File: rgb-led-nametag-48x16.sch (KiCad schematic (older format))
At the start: 44 parts, among them J1 USB_C_Receptacle_USB2.0, Q17 CJ3139K, Q18 CJ3139K, Q19 2SK3541, Q20 AO3401A, U25 STM32F722RETx, U26 SRV05-4, U27 TPS63001, U28 XC6206P332MR

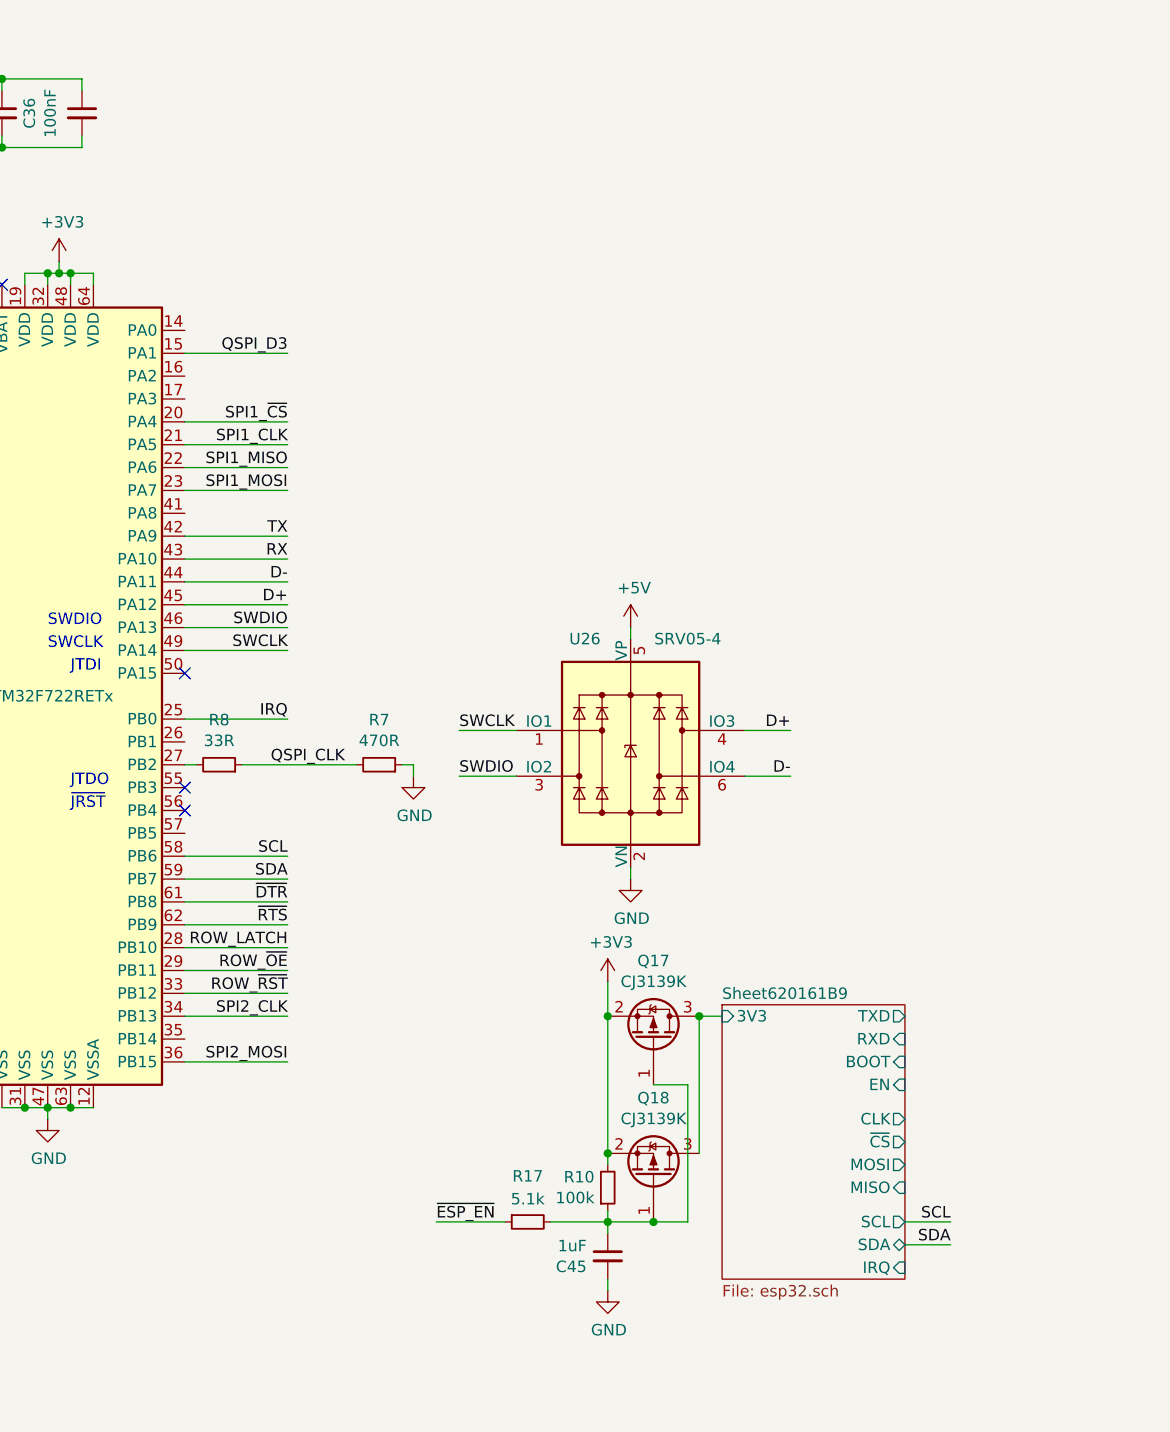
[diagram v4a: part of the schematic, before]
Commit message: Layout remaining busses
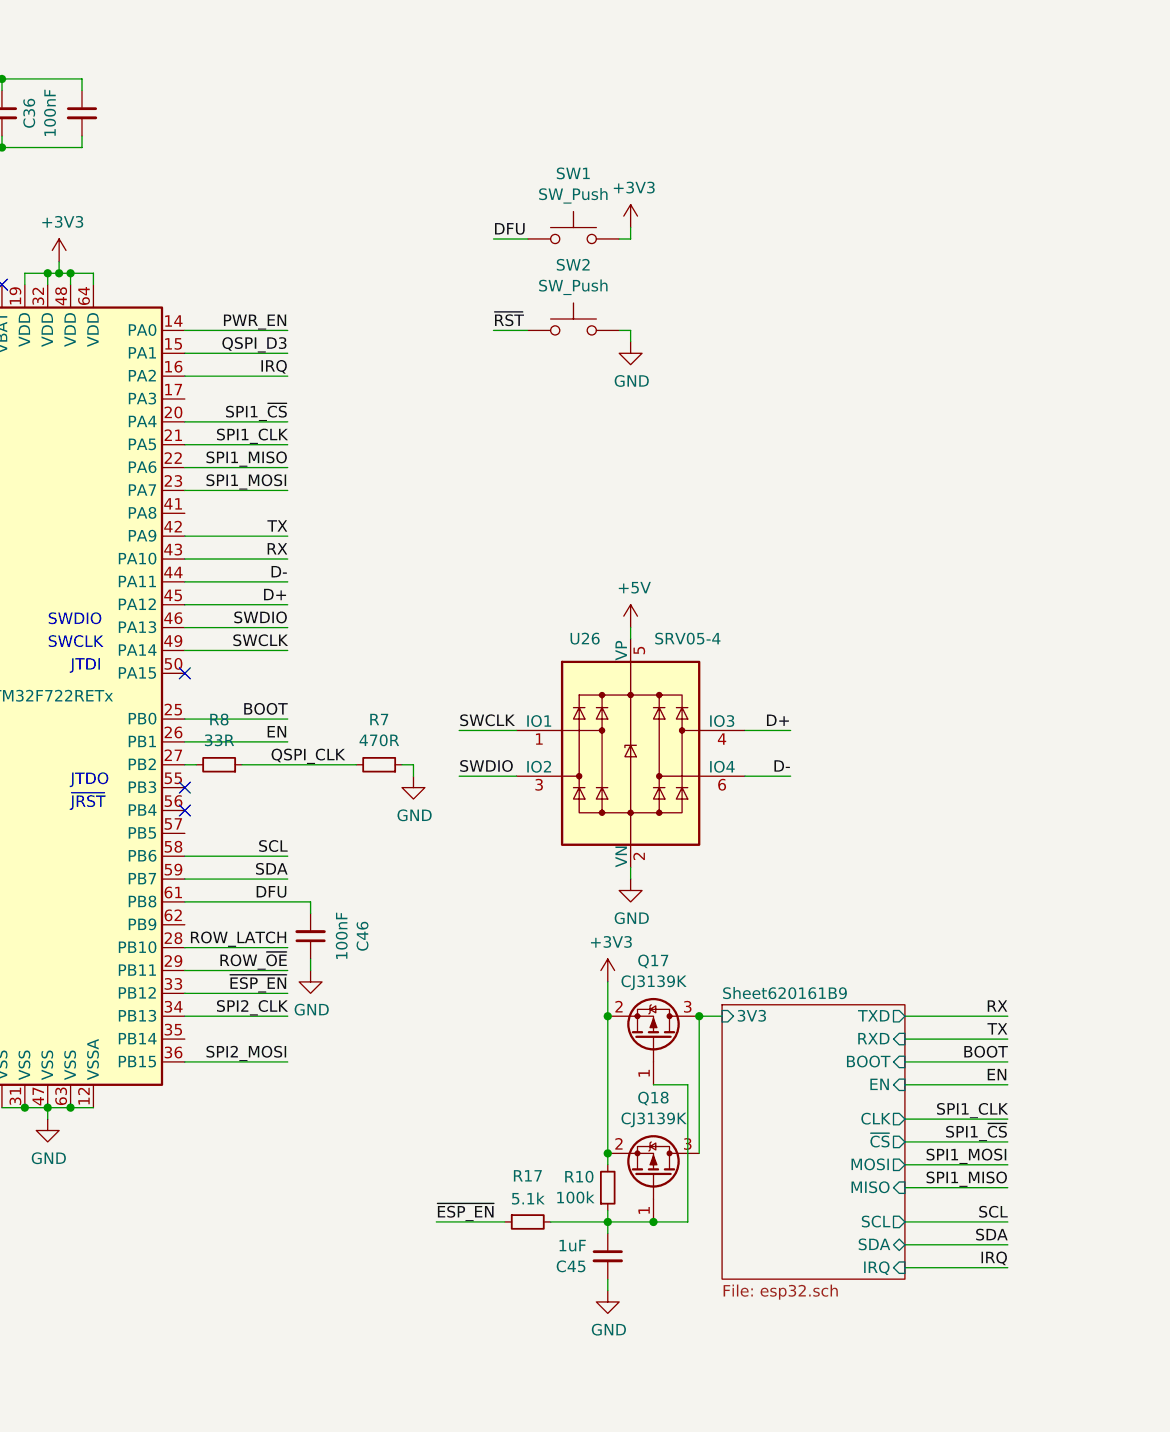
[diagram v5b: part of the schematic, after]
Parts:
- added C46: 100nF, Capacitor_SMD:C_0402_1005Metric, symbol Device:C_Small
- added SW1, SW2: SW_Push, Button_Switch_SMD:SW_Push_SPST_NO_Alps_SKRK, symbol Switch:SW_Push
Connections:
- net ROW_~RST is gone; now on net ~ESP_EN: U25.33 (PB12)
- net ~DTR is gone; now on net DFU: U25.61 (PB8)
- net +3V3: now also SW1.2
- net DFU: now also C46.2, SW1.1
- net GND: now also C46.1, SW2.2
- net IRQ: now also U25.16 (PA2); no longer U25.25 (PB0)
- net PWR_EN: now also U25.14 (PA0)
- net ~RST: now also SW2.1
- net EN: now reaches U25.26 (PB1)
- net ~RTS: no longer names the net of U25.62 (PB9)
- new net BOOT: U25.25 (PB0)
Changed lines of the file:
@@
 Text Label 7850 4450 2    50   ~ 0
 SDA
-Text Label 7850 4550 2    50   ~ 0
-~DTR
-Text Label 7850 4650 2    50   ~ 0
-~RTS
 Text Label 7850 3150 2    50   ~ 0
 D-
@@
 	7400 4450 7850 4450
 Wire Wire Line
-	7400 4550 7850 4550
-Wire Wire Line
-	7400 4650 7850 4650
-Wire Wire Line
 	7400 2750 7850 2750
 Wire Wire Line
@@
 Text Label 5650 4550 0    50   ~ 0
 COL_~RST
-Text Label 7850 4950 2    50   ~ 0
-ROW_~RST
-Wire Wire Line
-	7400 4950 7850 4950
 NoConn ~ 7400 3550
 Text Notes 6900 3550 0    50   ~ 0
@@
 NoConn ~ 7400 4150
 Wire Wire Line
-	7400 3750 7850 3750
-Text Label 7850 3750 2    50   ~ 0
+	7400 2250 7850 2250
+Text Label 7850 2250 2    50   ~ 0
 IRQ
 Wire Wire Line
@@
 	13250 950  13250 1000
 Connection ~ 13250 1000
-Text Label 10750 5950 2    50   ~ 0
+Text Label 11000 5950 2    50   ~ 0
 SCL
-Text Label 10750 6050 2    50   ~ 0
+Text Label 11000 6050 2    50   ~ 0
 SDA
-Wire Wire Line
-	10750 5950 10550 5950
-Wire Wire Line
-	10750 6050 10550 6050
 Wire Wire Line
 	14700 3600 15650 3600
@@
 Wire Wire Line
 	7400 5050 7850 5050
+Wire Wire Line
+	7400 4750 7850 4750
+Wire Wire Line
+	9350 4450 9350 4400
+Text Label 7850 5250 2    50   ~ 0
+SPI2_MOSI
+Wire Wire Line
+	7400 5250 7850 5250
+Wire Wire Line
+	7400 3850 7850 3850
+Text Label 11000 5350 2    50   ~ 0
+EN
+Text Label 7850 3850 2    50   ~ 0
+EN
 Text Label 7850 5050 2    50   ~ 0
 SPI2_CLK
-Wire Wire Line
-	7400 4750 7850 4750
 Text Label 7850 4750 2    50   ~ 0
 ROW_LATCH
 Wire Wire Line
-	9350 4450 9350 4400
+	7400 3750 7850 3750
+Text Label 7850 3750 2    50   ~ 0
+BOOT
+Text Label 11000 5250 2    50   ~ 0
+BOOT
+Text Label 11000 6150 2    50   ~ 0
+IRQ
+Text Label 11000 5500 2    50   ~ 0
+SPI1_CLK
+Text Label 11000 5600 2    50   ~ 0
+SPI1_~CS
+Text Label 11000 5800 2    50   ~ 0
+SPI1_MISO
+Text Label 11000 5700 2    50   ~ 0
+SPI1_MOSI
+Wire Wire Line
+	10550 5700 11000 5700
+Wire Wire Line
+	10550 5800 11000 5800
+Wire Wire Line
+	10550 5500 11000 5500
+Wire Wire Line
+	10550 5600 11000 5600
+Wire Wire Line
+	10550 5950 11000 5950
+Wire Wire Line
+	10550 6050 11000 6050
+Wire Wire Line
+	10550 6150 11000 6150
+Wire Wire Line
+	10550 5350 11000 5350
+Wire Wire Line
+	10550 5250 11000 5250
+Wire Wire Line
+	10550 5150 11000 5150
+Text Label 11000 5150 2    50   ~ 0
+TX
+Wire Wire Line
+	10550 5050 11000 5050
+Text Label 11000 5050 2    50   ~ 0
+RX
+Wire Wire Line
+	7400 4950 7850 4950
+Text Label 7850 4950 2    50   ~ 0
+~ESP_EN
+Wire Wire Line
+	7400 2050 7850 2050
+Text Label 7850 2050 2    50   ~ 0
+PWR_EN
+$Comp
+L Switch:SW_Push SW2
+U 1 1 630C4584
+P 9100 2050
+F 0 "SW2" H 9100 2335 50  0000 C CNN
+F 1 "SW_Push" H 9100 2244 50  0000 C CNN
+F 2 "Button_Switch_SMD:SW_Push_SPST_NO_Alps_SKRK" H 9100 2250 50  0001 C CNN
+F 3 "~" H 9100 2250 50  0001 C CNN
+F 4 "C115357" H 9100 2050 50  0001 C CNN "LCSC"
+	1    9100 2050
+	1    0    0    -1
+$EndComp
+$Comp
+L Switch:SW_Push SW1
+U 1 1 630C4D6E
+P 9100 1650
+F 0 "SW1" H 9100 1935 50  0000 C CNN
+F 1 "SW_Push" H 9100 1844 50  0000 C CNN
+F 2 "Button_Switch_SMD:SW_Push_SPST_NO_Alps_SKRK" H 9100 1850 50  0001 C CNN
+F 3 "~" H 9100 1850 50  0001 C CNN
+F 4 "C115357" H 9100 1650 50  0001 C CNN "LCSC"
+	1    9100 1650
+	1    0    0    -1
+$EndComp
+$Comp
+L power:GND #PWR0203
+U 1 1 630DD49F
+P 9350 2100
+F 0 "#PWR0203" H 9350 1850 50  0001 C CNN
+F 1 "GND" H 9355 1927 50  0000 C CNN
+F 2 "" H 9350 2100 50  0001 C CNN
+F 3 "" H 9350 2100 50  0001 C CNN
+	1    9350 2100
+	1    0    0    -1
+$EndComp
+Wire Wire Line
+	9350 2050 9300 2050
+Text Label 8750 2050 0    50   ~ 0
+~RST
+Wire Wire Line
+	8750 2050 8900 2050
+Text Label 8750 1650 0    50   ~ 0
+DFU
+Wire Wire Line
+	8750 1650 8900 1650
+Wire Wire Line
+	9350 2100 9350 2050
+$Comp
+L power:+3V3 #PWR0204
+U 1 1 631717FF
+P 9350 1600
+F 0 "#PWR0204" H 9350 1450 50  0001 C CNN
+F 1 "+3V3" H 9365 1773 50  0000 C CNN
+F 2 "" H 9350 1600 50  0001 C CNN
+F 3 "" H 9350 1600 50  0001 C CNN
+	1    9350 1600
+	1    0    0    -1
+$EndComp
+Wire Wire Line
+	9350 1600 9350 1650
+Wire Wire Line
+	9350 1650 9300 1650
+Text Label 7850 4550 2    50   ~ 0
+DFU
+$Comp
+L Device:C_Small C?
+U 1 1 631C20EA
+P 7950 4700
+AR Path="/61A41C1D/61A5C767/631C20EA" Ref="C?"  Part="1"
+AR Path="/61A41C1D/61A68DB0/631C20EA" Ref="C?"  Part="1"
+AR Path="/61A41C1D/61A6C361/631C20EA" Ref="C?"  Part="1"
+AR Path="/61A41C1D/61A75B5D/631C20EA" Ref="C?"  Part="1"
+AR Path="/61A41C1D/61A75B6D/631C20EA" Ref="C?"  Part="1"
+AR Path="/61A41C1D/61A75B93/631C20EA" Ref="C?"  Part="1"
+AR Path="/61C4C20D/61A5C767/631C20EA" Ref="C?"  Part="1"
+AR Path="/61C4C20D/61A68DB0/631C20EA" Ref="C?"  Part="1"
+AR Path="/61C4C20D/61A6C361/631C20EA" Ref="C?"  Part="1"
+AR Path="/61C4C20D/61A75B5D/631C20EA" Ref="C?"  Part="1"
+AR Path="/61C4C20D/61A75B6D/631C20EA" Ref="C?"  Part="1"
+AR Path="/61C4C20D/61A75B93/631C20EA" Ref="C?"  Part="1"
+AR Path="/61C4C905/61A5C767/631C20EA" Ref="C?"  Part="1"
+AR Path="/61C4C905/61A68DB0/631C20EA" Ref="C?"  Part="1"
+AR Path="/61C4C905/61A6C361/631C20EA" Ref="C?"  Part="1"
+AR Path="/61C4C905/61A75B5D/631C20EA" Ref="C?"  Part="1"
+AR Path="/61C4C905/61A75B6D/631C20EA" Ref="C?"  Part="1"
+AR Path="/61C4C905/61A75B93/631C20EA" Ref="C?"  Part="1"
+AR Path="/631C20EA" Ref="C46"  Part="1"
+F 0 "C46" V 7721 4700 50  0000 C CNN
+F 1 "100nF" V 7812 4700 50  0000 C CNN
+F 2 "Capacitor_SMD:C_0402_1005Metric" H 7950 4700 50  0001 C CNN
+F 3 "~" H 7950 4700 50  0001 C CNN
+F 4 "C1525" V 7950 4700 50  0001 C CNN "LCSC"
+	1    7950 4700
+	-1   0    0    1
+$EndComp
+Wire Wire Line
+	7950 4550 7950 4600
+Wire Wire Line
+	7400 4550 7950 4550
+$Comp
+L power:GND #PWR0205
+U 1 1 631F3184
+P 7950 4850
+F 0 "#PWR0205" H 7950 4600 50  0001 C CNN
+F 1 "GND" H 7955 4677 50  0000 C CNN
+F 2 "" H 7950 4850 50  0001 C CNN
+F 3 "" H 7950 4850 50  0001 C CNN
+	1    7950 4850
+	1    0    0    -1
+$EndComp
+Wire Wire Line
+	7950 4850 7950 4800
 Wire Bus Line
 	2950 1250 2950 6650
-Text Label 7850 5250 2    50   ~ 0
-SPI2_MOSI
-Wire Wire Line
-	7400 5250 7850 5250
 $EndSCHEMATC

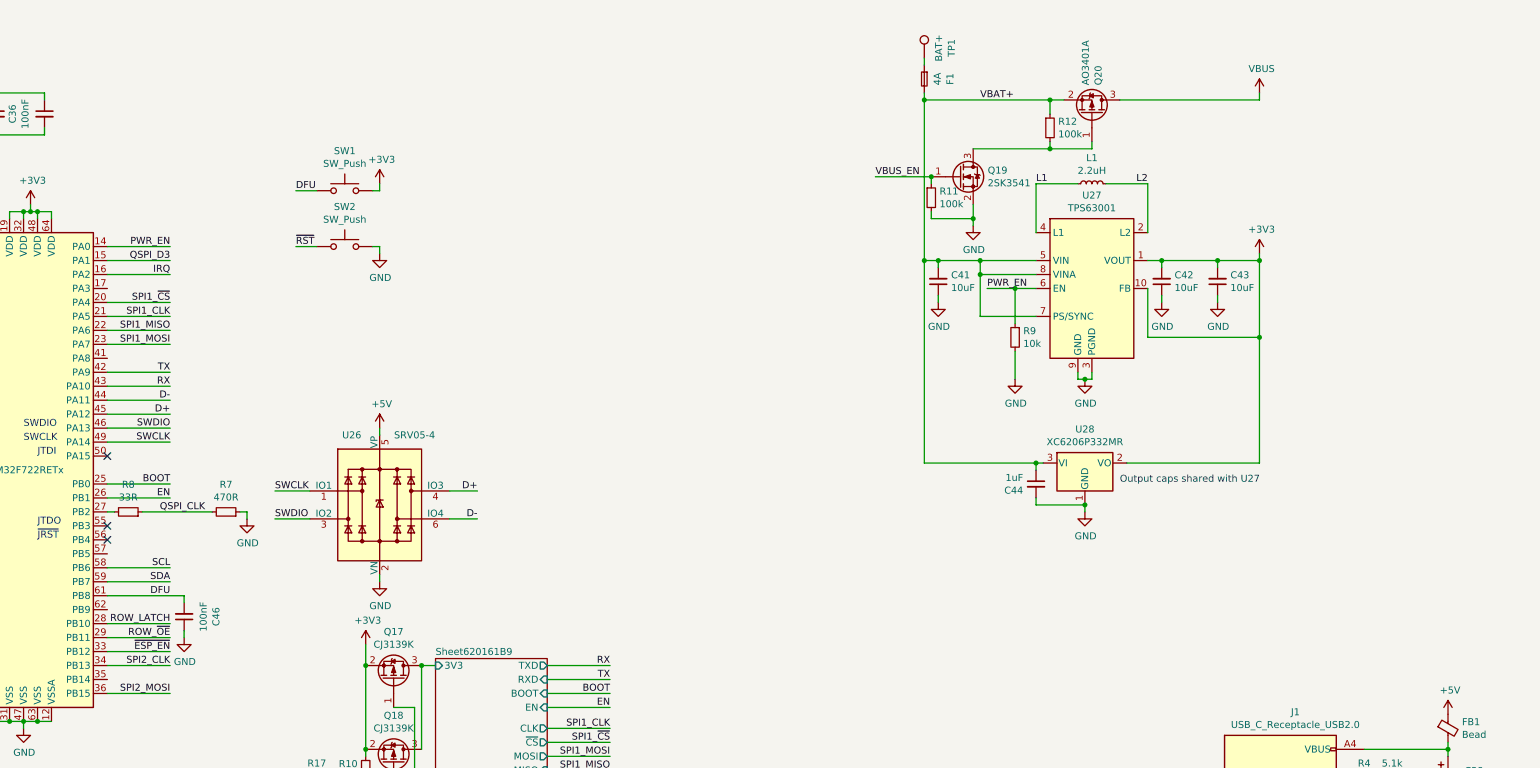
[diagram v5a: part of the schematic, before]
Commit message: Add primary battery protection
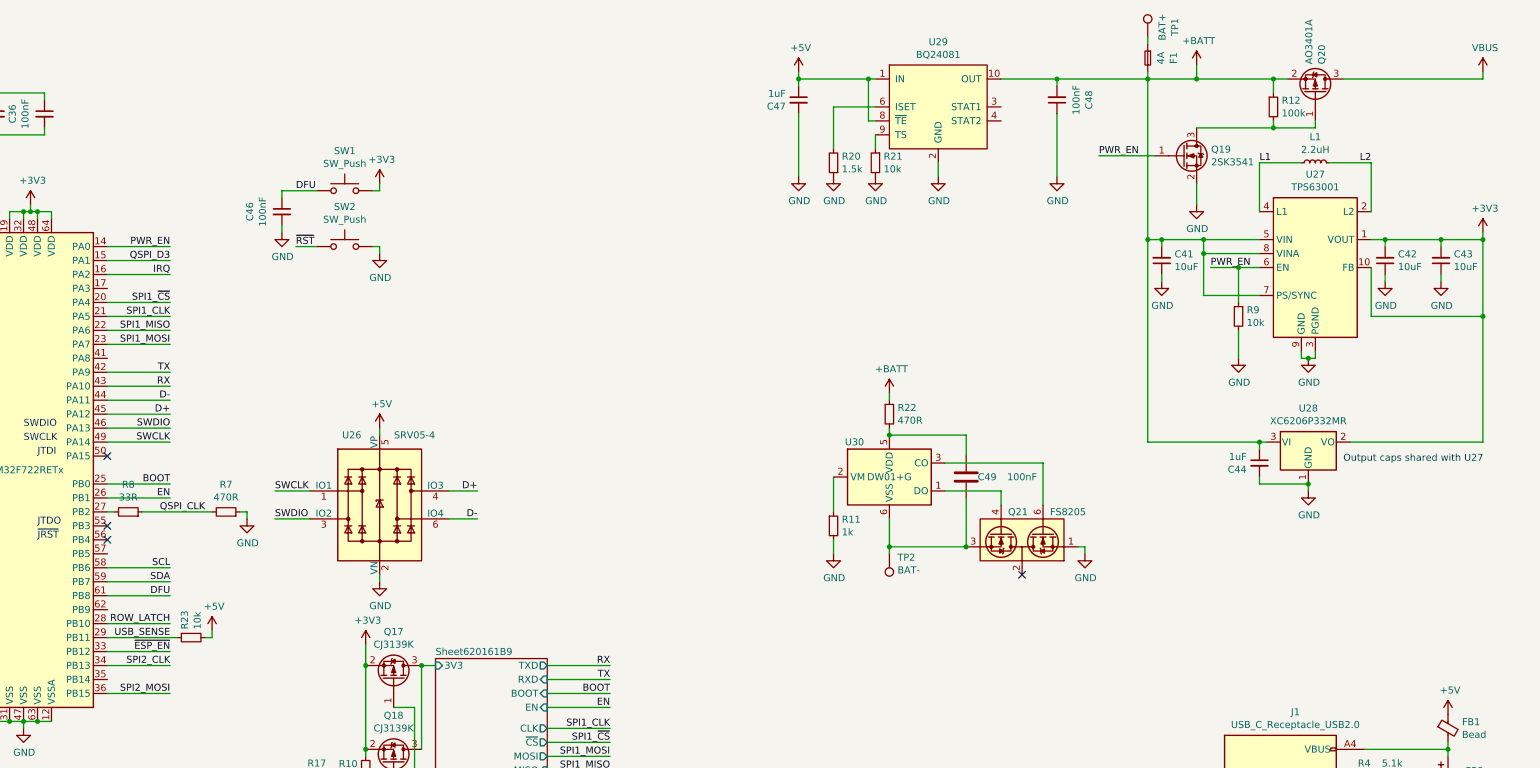
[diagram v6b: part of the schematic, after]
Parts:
- added C47: 1uF, Capacitor_SMD:C_0402_1005Metric, symbol Device:C_Small
- added C48: 100nF, Capacitor_SMD:C_0402_1005Metric, symbol Device:C_Small
- added C49: 100nF, Capacitor_SMD:C_0402_1005Metric, symbol Device:C
- added Q21: FS8205, Package_TO_SOT_SMD:SOT-23-6, symbol Transistor_FET_Dual:FS8205
- added R20: 1.5k, Resistor_SMD:R_0402_1005Metric, symbol Device:R_Small
- added R21, R23: 10k, Resistor_SMD:R_0402_1005Metric, symbol Device:R_Small
- added R22: 470R, Resistor_SMD:R_0603_1608Metric, symbol Device:R_Small
- added TP2: BAT-, TestPoint:TestPoint_Pad_2.0x2.0mm, symbol Connector:TestPoint
- added U29: BQ24081, Package_SON:Texas_DRC0010J_ThermalVias, symbol Battery_Management_TI:BQ24081
- added U30: DW01+G, Package_TO_SOT_SMD:SOT-23-6, symbol Battery_Management:AP9101CK6
- R11: value 100k -> 1k; LCSC C25741 -> C11702
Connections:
- net +5V: now also C47.1, R23.2, U29.1 (IN), U29.8 (~TE)
- net DFU: now also C46.1; no longer C46.2
- net GND: now also C46.2, C47.2, C48.1, Q21.1, R20.1, R21.2, U29.11 (GND), U29.2 (GND), U29.5 (GND), U29.7 (GND); no longer C46.1
- net PWR_EN: now also Q19.1 (G)
- net ROW_~OE renamed USB_SENSE
- net USB_SENSE: now also R23.1
- net VBAT+ renamed +BATT
- net +BATT: now also C48.2, R22.1, U29.10 (OUT)
- net VBUS_EN: no longer names the net of R11.1
- net VBUS_EN: now also U30.2 (VM); no longer Q19.1 (G)
- new net: R20.2, U29.6 (ISET)
- new net: R21.1, U29.9 (TS)
- new net: Q21.4, U30.1 (DO)
- new net: Q21.6, U30.3 (CO)
- new net: C49.2, R22.2, U30.5 (VDD)
- new net: C49.1, Q21.3, TP2.1, U30.6 (VSS)
- new net: Q21.2, Q21.5
- no-connect marks 7 -> 8
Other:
- moved on the sheet: C41, C42, C43, C44, C46, F1, L1, Q19, Q20, R12, R9, TP1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
